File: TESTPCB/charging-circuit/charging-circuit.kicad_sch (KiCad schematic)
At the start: 0 parts

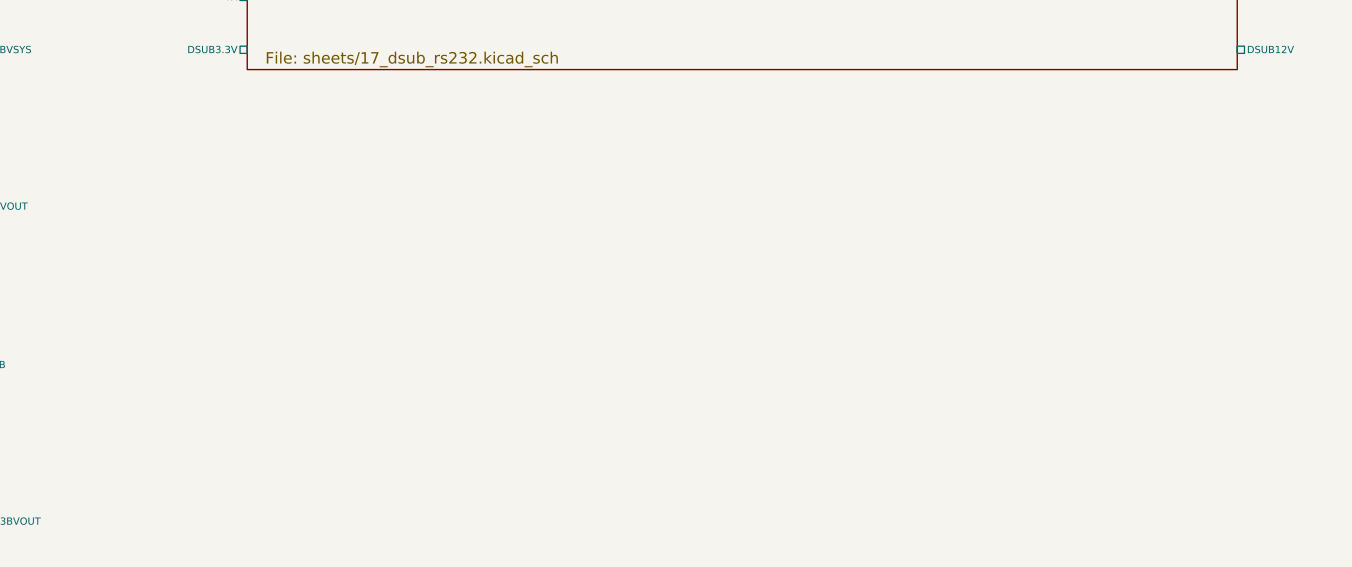
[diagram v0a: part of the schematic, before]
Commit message: Added LM2596 module to sheet
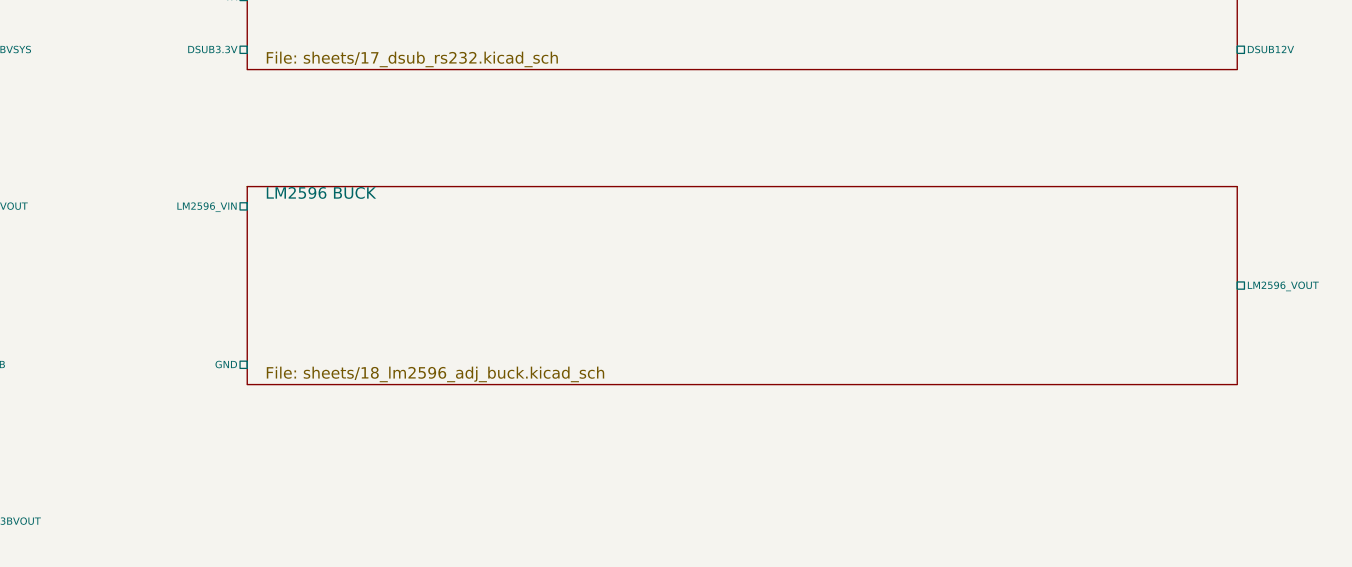
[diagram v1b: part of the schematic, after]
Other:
- added sheet LM2596 BUCK (sheets/18_lm2596_adj_buck.kicad_sch)
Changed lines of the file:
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@@
+		)
+	)
+	(sheet
+		(at 282.54 113.74)
+		(size 110 22)
+		(exclude_from_sim no)
+		(in_bom yes)
+		(on_board yes)
+		(dnp no)
+		(stroke
+			(width 0.1524)
+			(type solid)
+		)
+		(fill
+			(color 0 0 0 0.0000)
+		)
+		(property "Sheetname" "LM2596 BUCK"
+			(at 284.54 115.24 0)
+			(effects
+				(font
+					(size 1.27 1.27)
+				)
+				(justify left bottom)
+			)
+		)
+		(property "Sheetfile" "sheets/18_lm2596_adj_buck.kicad_sch"
+			(at 284.54 133.74 0)
+			(effects
+				(font
+					(size 1.27 1.27)
+				)
+				(justify left top)
+			)
+		)
+		(pin "LM2596_VIN" passive
+			(at 282.54 115.94 0)
+			(effects
+				(font
+					(size 0.8 0.8)
+				)
+			)
+		)
+		(pin "GND" passive
+			(at 282.54 133.54 0)
+			(effects
+				(font
+					(size 0.8 0.8)
+				)
+			)
+		)
+		(pin "LM2596_VOUT" passive
+			(at 392.54 124.74 180)
+			(effects
+				(font
+					(size 0.8 0.8)
+				)
+			)
 		)
 	)

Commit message: added 5V buck
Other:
- added sheet LM2596 5V Buck (sheets/18_lm2596_5V_buck.kicad_sch)

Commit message: Fixed formatting issues, now the hierachal sheets are all labeled as net labels and when we want to expose their pins we will make them into hierchal or global pins
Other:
- sheet 12BUCK ports: added none; removed 12BGND, 12BOOT, 12BVOUT, 12BVSYS, 12FB
- sheet 12VLDO ports: added none; removed 12GND, 12VOUT, 12VSYS
- sheet 3.3BUCK ports: added none; removed 3V3BGND, 3V3BOOT, 3V3BVOUT, 3V3BVSYS, 3V3FB
- sheet 3.3VLDO ports: added none; removed 3V3GND, 3V3VOUT, 3V3VSYS
- sheet 3S Balancer ports: added none; removed ALERT-2-RASPI, BAT_1 (+), BAT_1 (-), BAT_2 (+), BAT_2 (-), BAT_3 (+), BAT_3 (-), GND, PACK+, PACK-, PROTECT-, SCL-2-RASPI, SDA-2-RASPI, VC1, VCC
- sheet 3S IC ports: added none; removed 12V_Adapter, CHG_GND, CHG_VBAT, VREF
- sheet 5BUCK ports: added none; removed 5BGND, 5BOOT, 5BVOUT, 5BVSYS, 5FB
- sheet 5VLDO ports: added none; removed 5GND, 5VOUT, 5VSYS
- sheet CHARGE1 ports: added none; removed 1D+, 1D-, GND1, REGN1, VBAT1, VBUS1, VSYS1
- sheet DSUB+RS232 ports: added none; removed DSUB12V, DSUB3.3V, DSUBGND, RX, TX, UART_RX_13V, UART_TX_13V
- sheet FUELGAUGE ports: added none; removed FUELBAT, FUELGND, FUELSCL, FUELSDA
- sheet IC2 breakout ports: added none; removed 2D+, 2D-, BAT2, BTST, CE2, GND2, ICHG2, ILIM2, OTG2, PG2, PMID2, REGN2, STAT2, SW2, SYS2, TS2, VAC2, VBUS2, VSET2
- sheet LM2596 5V Buck ports: added none; removed GND, LM2596_5V_VIN, LM2596_5V_VOUT
- sheet LM2596 BUCK ports: added none; removed GND, LM2596_VIN, LM2596_VOUT
- sheet SLEEPMOSFET ports: added none; removed SLEEPGND, SLEEPSIG, SLEEPVSYS
- sheet TEMP+HEATER ports: added none; removed A0, A1, A2, A3, Address, PWMSIG, TEMP12V, TEMPGND, TEMPSCL, TEMPSDA, Temp3.3V, base
- sheet USB+BAT ports: added none; removed D+, D-, USBGND, VBAT, VBUS
- sheet USBC-PD ports: added none; removed CC1, CC2, ISET, PDGND, PDVOUT, VSET
- sheet V1 IC ports: added none; removed V1GND, V1VBAT, V1VBUS, V1VSYS
